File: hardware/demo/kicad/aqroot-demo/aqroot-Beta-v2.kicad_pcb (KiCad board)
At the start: 6 copper layers, 72 x 148 mm, 311 parts, among them J1 FH69-50S-0.5SH, J2 Molex_5025700893, J3 USB_C_Receptacle_USB2.0_16P, J4 JST-PH-2 BATTERY, J5 COMMUNITY_PORT_1x24, J6 JST-PH-2 SPEAKER, J7 BM02B-ACHSS-GAN-ETF, J8 QWIIC_STEMMA_QT, Q1 AO3400A, Q10 2N7002, Q2 NTMD4820N, Q3 NTMD4820N, Q4 BSS138, Q5 AO3401A, Q6 BSS138, Q7 BSS138, Q8 BSS138, Q9 BSS138, SW1 BOOT, SW2 UP, SW3 DOWN, SW4 LEFT, SW5 RIGHT, SW6 A_SELECT, SW7 B_BACK, SW9 SW_SPDT, U1 ESP32-S3-WROOM-1, U10 USBLC6-2SC6, U11 BQ25185, U12 TPS63020, U13 TPS61023, U14 MAX17048, U16 TCA4307DGKR, U17 TPS61169DCKR, U18 LTC4368-1, U19 TLV7032, U2 PCAL9535APW, U20 TPS22950C, U21 TPS61023, U22 TPS22950C, U3 PCAL9535APW, U4 BMI270, U5 MAX98357A, U6 TSOP38238, U7 E07-400M10S, U8 E22-900M22S, U9 ST25R3916-AQET, Y1 27.12MHz 10pF 3225-4P

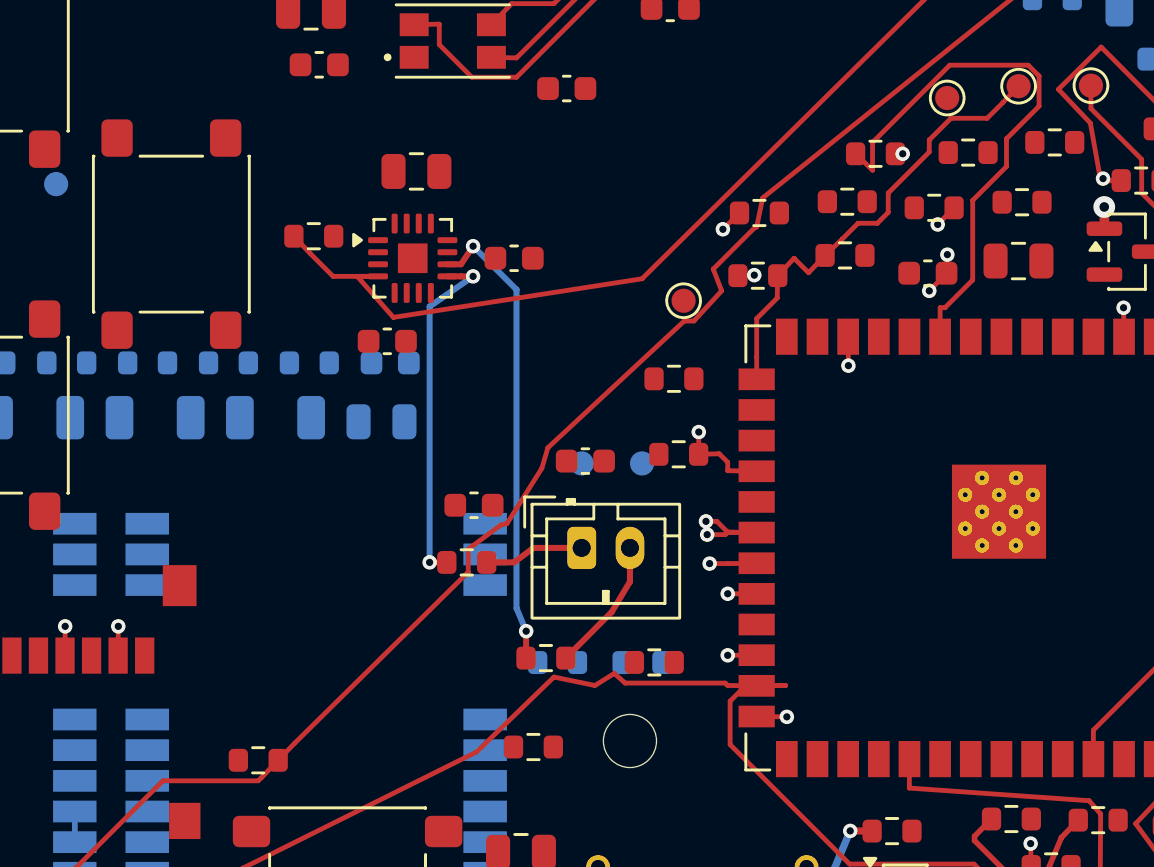
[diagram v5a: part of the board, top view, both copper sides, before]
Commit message: demo: route CC1101 chip select tree
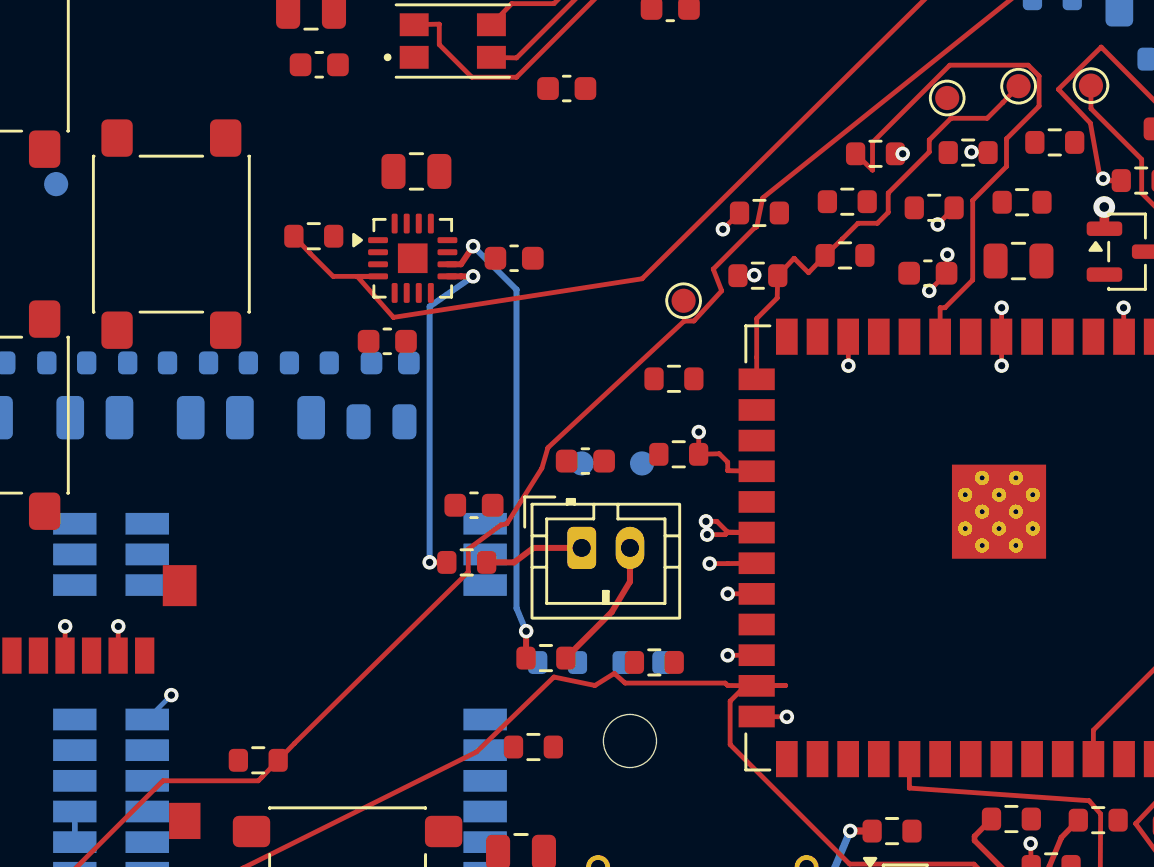
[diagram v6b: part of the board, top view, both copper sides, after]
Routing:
- net /CC1101_CS_N: track 0.00 -> 49.4 mm, vias 0 -> 4
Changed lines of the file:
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@@
+	)
+	(segment
+		(start 54 111.6)
+		(end 54.15 111.6)
+		(width 0.2)
+		(layer "F.Cu")
+		(net "/CC1101_CS_N")
+	)
+	(segment
+		(start 54.836648 111.621211)
+		(end 54 111.6)
+		(width 0.2)
+		(layer "F.Cu")
+		(net "/CC1101_CS_N")
+	)
+	(segment
+		(start 55.39 119.25)
+		(end 55.4 120.45)
+		(width 0.2)
+		(layer "F.Cu")
+		(net "/CC1101_CS_N")
+	)
+	(segment
+		(start 55.39 119.25)
+		(end 55.4 118.05)
+		(width 0.2)
+		(layer "F.Cu")
+		(net "/CC1101_CS_N")
+	)
+	(via
+		(at 21 134.1)
+		(size 0.6)
+		(drill 0.3)
+		(layers "F.Cu" "B.Cu")
+		(net "/CC1101_CS_N")
+	)
+	(via
+		(at 55.4 120.45)
+		(size 0.6)
+		(drill 0.3)
+		(layers "F.Cu" "B.Cu")
+		(net "/CC1101_CS_N")
+	)
+	(via
+		(at 54.15 111.6)
+		(size 0.6)
+		(drill 0.3)
+		(layers "F.Cu" "B.Cu")
+		(net "/CC1101_CS_N")
+	)
+	(via
+		(at 55.4 118.05)
+		(size 0.6)
+		(drill 0.3)
+		(layers "F.Cu" "B.Cu")
+		(net "/CC1101_CS_N")
+	)
+	(segment
+		(start 20 135.11)
+		(end 21 134.1)
+		(width 0.2)
+		(layer "B.Cu")
+		(net "/CC1101_CS_N")
+	)
+	(segment
+		(start 55.4 118.05)
+		(end 54.15 111.6)
+		(width 0.2)
+		(layer "In2.Cu")
+		(net "/CC1101_CS_N")
+	)
+	(segment
+		(start 39.35 122.1)
+		(end 21 134.1)
+		(width 0.2)
+		(layer "In3.Cu")
+		(net "/CC1101_CS_N")
+	)
+	(segment
+		(start 55.4 120.45)
+		(end 39.35 122.1)
+		(width 0.2)
+		(layer "In3.Cu")
+		(net "/CC1101_CS_N")
 	)
 	(segment

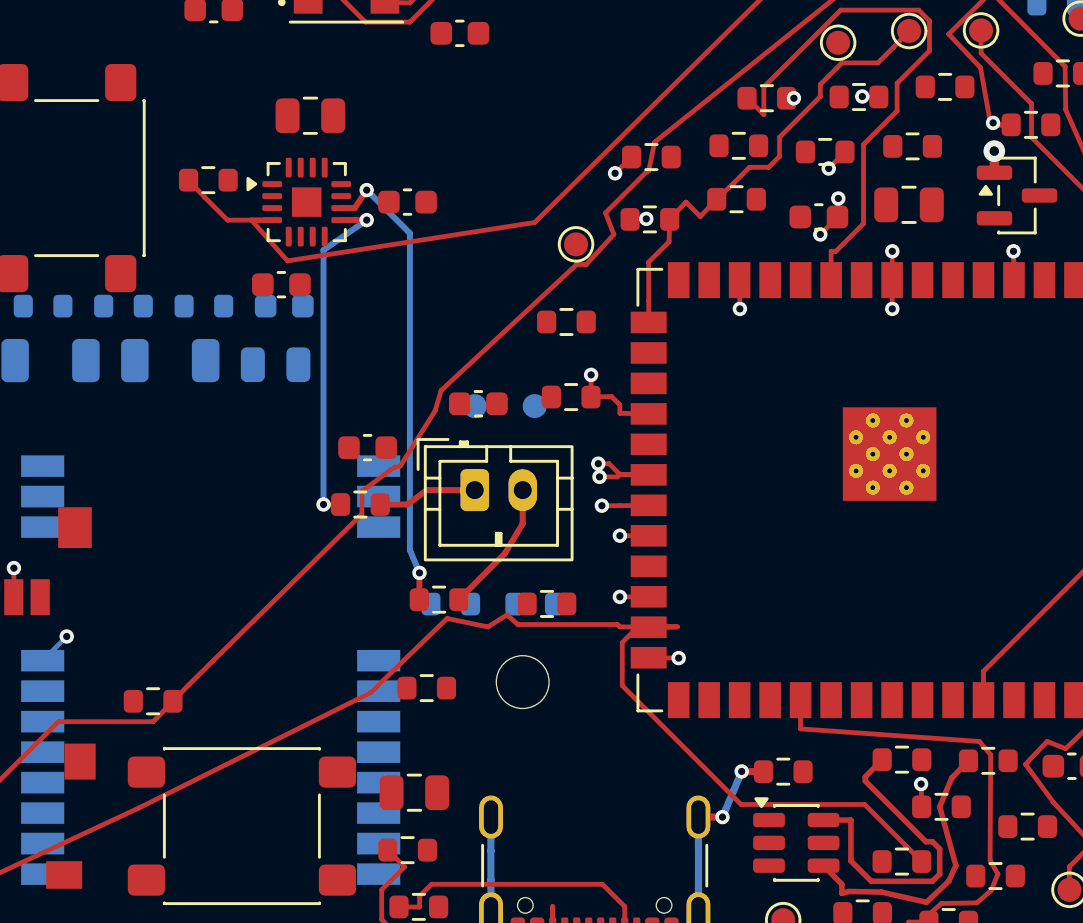
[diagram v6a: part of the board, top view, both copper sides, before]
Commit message: demo: route BOOT recovery tree
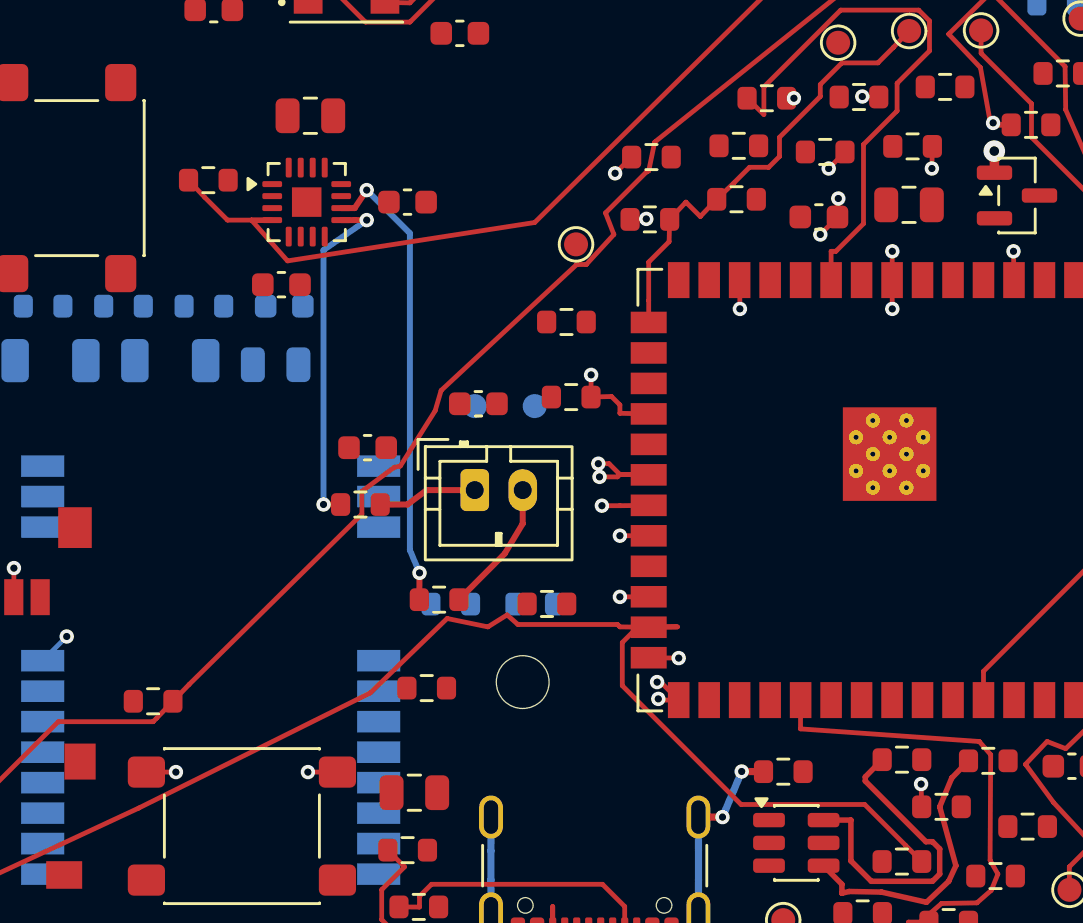
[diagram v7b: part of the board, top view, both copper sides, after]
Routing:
- net /02_MCU_CORE/BOOT_N: track 0.00 -> 63.3 mm, vias 0 -> 5
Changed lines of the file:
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@@
+	)
+	(segment
+		(start 32.28 139.75)
+		(end 31.05 139.75)
+		(width 0.2)
+		(layer "F.Cu")
+		(net "/02_MCU_CORE/BOOT_N")
+	)
+	(segment
+		(start 57.06979 113.678884)
+		(end 57.05 114.6)
+		(width 0.2)
+		(layer "F.Cu")
+		(net "/02_MCU_CORE/BOOT_N")
+	)
+	(segment
+		(start 24.32 139.75)
+		(end 25.55 139.75)
+		(width 0.2)
+		(layer "F.Cu")
+		(net "/02_MCU_CORE/BOOT_N")
+	)
+	(segment
+		(start 46.5 136.75)
+		(end 45.6 135.85)
+		(width 0.2)
+		(layer "F.Cu")
+		(net "/02_MCU_CORE/BOOT_N")
+	)
+	(segment
+		(start 45.6 135.85)
+		(end 45.6 136)
+		(width 0.2)
+		(layer "F.Cu")
+		(net "/02_MCU_CORE/BOOT_N")
+	)
+	(segment
+		(start 46.5 136.75)
+		(end 45.6 136.75)
+		(width 0.2)
+		(layer "F.Cu")
+		(net "/02_MCU_CORE/BOOT_N")
+	)
+	(segment
+		(start 45.6 136.75)
+		(end 45.65 136.7)
+		(width 0.2)
+		(layer "F.Cu")
+		(net "/02_MCU_CORE/BOOT_N")
+	)
+	(via
+		(at 45.6 136)
+		(size 0.6)
+		(drill 0.3)
+		(layers "F.Cu" "B.Cu")
+		(net "/02_MCU_CORE/BOOT_N")
+	)
+	(via
+		(at 31.05 139.75)
+		(size 0.6)
+		(drill 0.3)
+		(layers "F.Cu" "B.Cu")
+		(net "/02_MCU_CORE/BOOT_N")
+	)
+	(via
+		(at 57.05 114.6)
+		(size 0.6)
+		(drill 0.3)
+		(layers "F.Cu" "B.Cu")
+		(net "/02_MCU_CORE/BOOT_N")
+	)
+	(via
+		(at 25.55 139.75)
+		(size 0.6)
+		(drill 0.3)
+		(layers "F.Cu" "B.Cu")
+		(net "/02_MCU_CORE/BOOT_N")
+	)
+	(via
+		(at 45.65 136.7)
+		(size 0.6)
+		(drill 0.3)
+		(layers "F.Cu" "B.Cu")
+		(net "/02_MCU_CORE/BOOT_N")
+	)
+	(segment
+		(start 45.65 136.7)
+		(end 42.6 139.75)
+		(width 0.2)
+		(layer "In2.Cu")
+		(net "/02_MCU_CORE/BOOT_N")
+	)
+	(segment
+		(start 42.6 139.75)
+		(end 25.55 139.75)
+		(width 0.2)
+		(layer "In2.Cu")
+		(net "/02_MCU_CORE/BOOT_N")
+	)
+	(segment
+		(start 31.05 139.75)
+		(end 25.55 139.75)
+		(width 0.2)
+		(layer "In2.Cu")
+		(net "/02_MCU_CORE/BOOT_N")
+	)
+	(segment
+		(start 60.175 118.625)
+		(end 60.6 118.8)
+		(width 0.2)
+		(layer "In3.Cu")
+		(net "/02_MCU_CORE/BOOT_N")
+	)
+	(segment
+		(start 61.35 118.05)
+		(end 57.4 114.25)
+		(width 0.2)
+		(layer "In3.Cu")
+		(net "/02_MCU_CORE/BOOT_N")
+	)
+	(segment
+		(start 60.6 118.8)
+		(end 61.35 118.05)
+		(width 0.2)
+		(layer "In3.Cu")
+		(net "/02_MCU_CORE/BOOT_N")
+	)
+	(segment
+		(start 57.4 114.25)
+		(end 57.05 114.6)
+		(width 0.2)
+		(layer "In3.Cu")
+		(net "/02_MCU_CORE/BOOT_N")
+	)
+	(segment
+		(start 46.525 132.25)
+		(end 60.175 118.625)
+		(width 0.2)
+		(layer "In3.Cu")
+		(net "/02_MCU_CORE/BOOT_N")
+	)
+	(segment
+		(start 45.6 136)
+		(end 46.525 132.25)
+		(width 0.2)
+		(layer "In3.Cu")
+		(net "/02_MCU_CORE/BOOT_N")
 	)
 	(segment

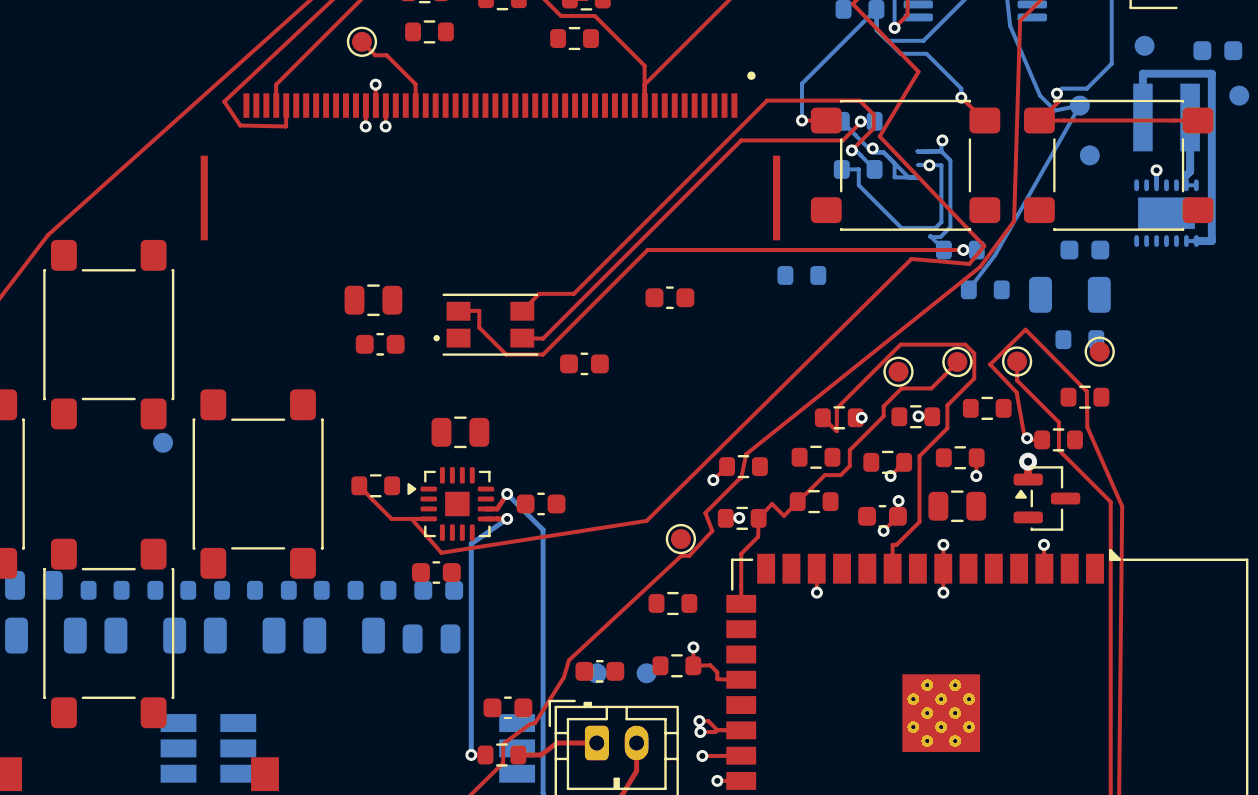
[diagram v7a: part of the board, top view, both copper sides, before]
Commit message: demo: route TPS63020 power-good tree
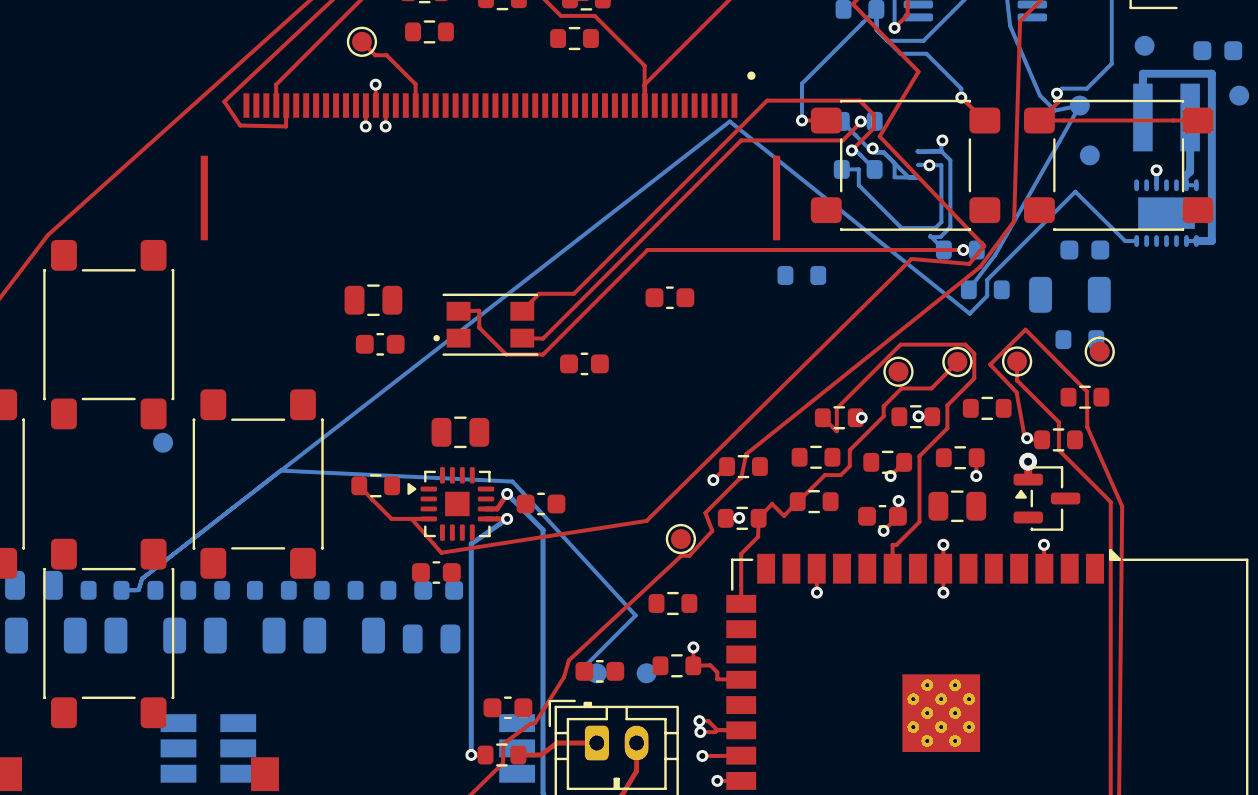
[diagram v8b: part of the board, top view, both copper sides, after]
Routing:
- net Net-(U12-PG): track 0.00 -> 102.8 mm
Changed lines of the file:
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@@
+	)
+	(segment
+		(start 33.775 114.875)
+		(end 39.95 121.6)
+		(width 0.2)
+		(layer "B.Cu")
+		(net "Net-(U12-PG)")
+	)
+	(segment
+		(start 22.125 114.325)
+		(end 33.775 114.875)
+		(width 0.2)
+		(layer "B.Cu")
+		(net "Net-(U12-PG)")
+	)
+	(segment
+		(start 15 120.325)
+		(end 15.175 119.75)
+		(width 0.2)
+		(layer "B.Cu")
+		(net "Net-(U12-PG)")
+	)
+	(segment
+		(start 38 124.5)
+		(end 37.05 124.5)
+		(width 0.2)
+		(layer "B.Cu")
+		(net "Net-(U12-PG)")
+	)
+	(segment
+		(start 15 120.325)
+		(end 15.175 119.75)
+		(width 0.2)
+		(layer "B.Cu")
+		(net "Net-(U12-PG)")
+	)
+	(segment
+		(start 57.6 105.55)
+		(end 57.6 104.75)
+		(width 0.2)
+		(layer "B.Cu")
+		(net "Net-(U12-PG)")
+	)
+	(segment
+		(start 56.725 106.45)
+		(end 57.6 105.55)
+		(width 0.2)
+		(layer "B.Cu")
+		(net "Net-(U12-PG)")
+	)
+	(segment
+		(start 14.14 120.335)
+		(end 15 120.325)
+		(width 0.2)
+		(layer "B.Cu")
+		(net "Net-(U12-PG)")
+	)
+	(segment
+		(start 57.6 104.75)
+		(end 62.025 100.325)
+		(width 0.2)
+		(layer "B.Cu")
+		(net "Net-(U12-PG)")
+	)
+	(segment
+		(start 44.675 96.8)
+		(end 56.725 106.45)
+		(width 0.2)
+		(layer "B.Cu")
+		(net "Net-(U12-PG)")
+	)
+	(segment
+		(start 15.175 119.75)
+		(end 22.125 114.325)
+		(width 0.2)
+		(layer "B.Cu")
+		(net "Net-(U12-PG)")
+	)
+	(segment
+		(start 14.14 120.335)
+		(end 15 120.325)
+		(width 0.2)
+		(layer "B.Cu")
+		(net "Net-(U12-PG)")
+	)
+	(segment
+		(start 39.95 121.6)
+		(end 37.05 124.5)
+		(width 0.2)
+		(layer "B.Cu")
+		(net "Net-(U12-PG)")
+	)
+	(segment
+		(start 62.025 100.325)
+		(end 64.525 102.8)
+		(width 0.2)
+		(layer "B.Cu")
+		(net "Net-(U12-PG)")
+	)
+	(segment
+		(start 15.175 119.75)
+		(end 44.675 96.8)
+		(width 0.2)
+		(layer "B.Cu")
+		(net "Net-(U12-PG)")
+	)
+	(segment
+		(start 65.1 102.8)
+		(end 64.525 102.8)
+		(width 0.2)
+		(layer "B.Cu")
+		(net "Net-(U12-PG)")
 	)
 	(segment
